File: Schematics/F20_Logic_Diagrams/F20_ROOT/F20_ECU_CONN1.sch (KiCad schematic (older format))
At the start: 1 part

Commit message: 02/18/20 update
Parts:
- gave numbers to parts that had none: 1
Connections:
- no-connect marks 0 -> 10
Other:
- moved on the sheet: U2
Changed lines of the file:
@@
 $Descr A 11000 8500
 encoding utf-8
-Sheet 3 11
+Sheet 3 13
 Title "ECU Connector 1"
 Date ""
@@
 $EndDescr
 $Comp
-L FSAE_Library:ECU_Conn1 U?
+L FSAE_Library:ECU_Conn1 U2
 U 1 1 5E3C649A
-P 4000 1000
-F 0 "U?" H 4750 1173 50  0000 C CNN
-F 1 "ECU_Conn1" H 4750 1150 50  0001 C CNN
-F 2 "" H 4500 2000 50  0001 C CNN
-F 3 "" H 4500 2000 50  0001 C CNN
-F 4 "https://www.molex.com/molex/products/part-detail/pcb_headers/0313872034" H 3950 1400 50  0001 C CNN "Header Datasheet"
-F 5 "https://www.molex.com/molex/products/part-detail/crimp_housings/0345660203" H 4000 1500 50  0001 C CNN "Plug Datasheet"
-	1    4000 1000
+P 4500 1000
+F 0 "U2" H 5250 1173 50  0000 C CNN
+F 1 "ECU_Conn1" H 5250 1150 50  0001 C CNN
+F 2 "" H 5000 2000 50  0001 C CNN
+F 3 "" H 5000 2000 50  0001 C CNN
+F 4 "https://www.molex.com/molex/products/part-detail/pcb_headers/0313872034" H 4450 1400 50  0001 C CNN "Header Datasheet"
+F 5 "https://www.molex.com/molex/products/part-detail/crimp_housings/0345660203" H 4500 1500 50  0001 C CNN "Plug Datasheet"
+	1    4500 1000
 	1    0    0    -1
 $EndComp
-Text GLabel 7500 1450 2    50   Output ~ 0
+Text GLabel 8000 1450 2    50   Output ~ 0
 ECU_+5V_Aux_Out1
-Text GLabel 2000 1450 0    50   Output ~ 0
+Text GLabel 2500 1450 0    50   Output ~ 0
 O2_SNSR_HEAT
-Text GLabel 2000 1900 0    50   Output ~ 0
+Text GLabel 2500 1900 0    50   Output ~ 0
 OS_SNSR_NVOLT
-Text GLabel 2000 1750 0    50   Output ~ 0
+Text GLabel 2500 1750 0    50   Output ~ 0
 O2_SNSR_IPUMP
-Text GLabel 2000 2050 0    50   Output ~ 0
+Text GLabel 2500 2050 0    50   Output ~ 0
 O2_SNSR_VGND
-Text GLabel 2000 1600 0    50   Output ~ 0
+Text GLabel 2500 1600 0    50   Output ~ 0
 O2_SNSR_ITRIM
 Wire Wire Line
-	2000 1450 4000 1450
+	2500 1450 4500 1450
 Wire Wire Line
-	4000 1600 2000 1600
+	4500 1600 2500 1600
 Wire Wire Line
-	2000 1750 4000 1750
+	2500 1750 4500 1750
 Wire Wire Line
-	4000 1900 2000 1900
+	4500 1900 2500 1900
 Wire Wire Line
-	2000 2050 4000 2050
+	2500 2050 4500 2050
 Wire Wire Line
-	7500 1450 5500 1450
+	8000 1450 6000 1450
 Wire Wire Line
-	5500 4450 7000 4450
+	6000 4450 7500 4450
 Wire Wire Line
-	5500 4900 7000 4900
+	6000 4900 7500 4900
 Wire Wire Line
-	7000 4900 7000 4450
-Connection ~ 7000 4450
+	7500 4900 7500 4450
+Connection ~ 7500 4450
 Wire Wire Line
-	7000 4450 7500 4450
-Text GLabel 7500 4450 2    50   Input ~ 0
+	7500 4450 8000 4450
+Text GLabel 8000 4450 2    50   Input ~ 0
 ECU_+12V_RLY
-Text GLabel 2000 5200 0    50   Input ~ 0
+Text GLabel 2500 5200 0    50   Input ~ 0
 ECU_RLY_CTRL_OUT
 Wire Wire Line
-	2000 5200 4000 5200
+	2500 5200 4500 5200
 $Comp
-L FSAE_Library:GND_BAT #PWR?
+L FSAE_Library:GND_BAT #PWR02
 U 1 1 5E44A710
-P 7500 6500
-F 0 "#PWR?" H 7500 6250 50  0001 C CNN
-F 1 "GND_BAT" H 7505 6327 50  0000 C CNN
-F 2 "" H 7500 6500 50  0001 C CNN
-F 3 "" H 7500 6500 50  0001 C CNN
-	1    7500 6500
+P 6500 6450
+F 0 "#PWR02" H 6500 6200 50  0001 C CNN
+F 1 "GND_BAT" H 6505 6277 50  0000 C CNN
+F 2 "" H 6500 6450 50  0001 C CNN
+F 3 "" H 6500 6450 50  0001 C CNN
+	1    6500 6450
 	1    0    0    -1
 $EndComp
 Wire Wire Line
-	7500 6500 7500 6250
+	6500 6450 6500 6250
 Wire Wire Line
-	7500 6250 6000 6250
+	6000 3550 6500 3550
 Wire Wire Line
-	5500 3550 6000 3550
+	6500 3550 6500 4300
+Connection ~ 6500 6250
 Wire Wire Line
-	6000 3550 6000 4300
-Connection ~ 6000 6250
+	6500 6250 6000 6250
 Wire Wire Line
-	6000 6250 5500 6250
+	6000 4300 6500 4300
+Connection ~ 6500 4300
 Wire Wire Line
-	5500 4300 6000 4300
-Connection ~ 6000 4300
+	4500 5350 4000 5350
 Wire Wire Line
-	6000 4300 6000 6250
-Wire Wire Line
-	4000 5350 3500 5350
-Wire Wire Line
-	3500 5350 3500 6500
+	4000 5350 4000 6500
 $Comp
-L FSAE_Library:GND_BAT #PWR?
+L FSAE_Library:GND_BAT #PWR03
 U 1 1 5E4538FC
-P 3500 6500
-F 0 "#PWR?" H 3500 6250 50  0001 C CNN
-F 1 "GND_BAT" H 3505 6327 50  0000 C CNN
-F 2 "" H 3500 6500 50  0001 C CNN
-F 3 "" H 3500 6500 50  0001 C CNN
-	1    3500 6500
+P 4000 6500
+F 0 "#PWR03" H 4000 6250 50  0001 C CNN
+F 1 "GND_BAT" H 4005 6327 50  0000 C CNN
+F 2 "" H 4000 6500 50  0001 C CNN
+F 3 "" H 4000 6500 50  0001 C CNN
+	1    4000 6500
 	1    0    0    -1
 $EndComp
-Text GLabel 2000 2350 0    50   Input ~ 0
+Text GLabel 2500 2350 0    50   Input ~ 0
 ECU_+12V_BAT
 Wire Wire Line
-	2000 2350 4000 2350
+	2500 2350 4500 2350
 Wire Wire Line
-	5500 5050 7500 5050
-Text Notes 8150 5200 0    50   ~ 0
+	6000 5050 8000 5050
+Text Notes 8650 5200 0    50   ~ 0
 SEEMS LIKE ITS JUST CONNECTED\nSTRAIGHT TO BATTERY...\nONE PART IN ECU DOC SAYS PUT 3A FUSE\nBUT IN OTHER THERE IS NO FUSE ...
-Text GLabel 7500 5050 2    50   Input ~ 0
+Text GLabel 8000 5050 2    50   Input ~ 0
 ECU_+12V_IGN
+NoConn ~ 6000 6100
+Wire Wire Line
+	6500 4300 6500 6250
+NoConn ~ 6000 5950
+NoConn ~ 6000 5800
+NoConn ~ 6000 5650
+NoConn ~ 6000 3700
+NoConn ~ 6000 3850
+NoConn ~ 6000 3400
+NoConn ~ 6000 3250
+NoConn ~ 4500 3100
+NoConn ~ 4500 3250
 $EndSCHEMATC

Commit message: 02/19/20 update
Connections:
- net COIL4_CTRL: now reaches U2.11 (Coil3_Out)
- net COIL3_CTRL: now reaches U2.12 (Coil2_Out)
- net COIL2_CTRL: now reaches U2.13 (Coil1_Out)
- net COIL1_CTRL: now reaches U2.14 (Coil0_Out)
- net ECU_+5V_Aux_Out1: no longer names the net of U2.41 (+5V_Aux_Out)
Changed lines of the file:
@@
 	1    0    0    -1
 $EndComp
-Text GLabel 8000 1450 2    50   Output ~ 0
-ECU_+5V_Aux_Out1
 Text GLabel 2500 1450 0    50   Output ~ 0
 O2_SNSR_HEAT
@@
 Wire Wire Line
 	2500 2050 4500 2050
-Wire Wire Line
-	8000 1450 6000 1450
 Wire Wire Line
 	6000 4450 7500 4450
@@
 NoConn ~ 4500 3100
 NoConn ~ 4500 3250
+Text GLabel 2500 2950 0    50   Output ~ 0
+COIL1_CTRL
+Text GLabel 2500 2800 0    50   Output ~ 0
+COIL2_CTRL
+Text GLabel 2500 2650 0    50   Output ~ 0
+COIL3_CTRL
+Text GLabel 2500 2500 0    50   Output ~ 0
+COIL4_CTRL
+Wire Wire Line
+	2500 2500 4500 2500
+Wire Wire Line
+	4500 2650 2500 2650
+Wire Wire Line
+	2500 2800 4500 2800
+Wire Wire Line
+	4500 2950 2500 2950
 $EndSCHEMATC

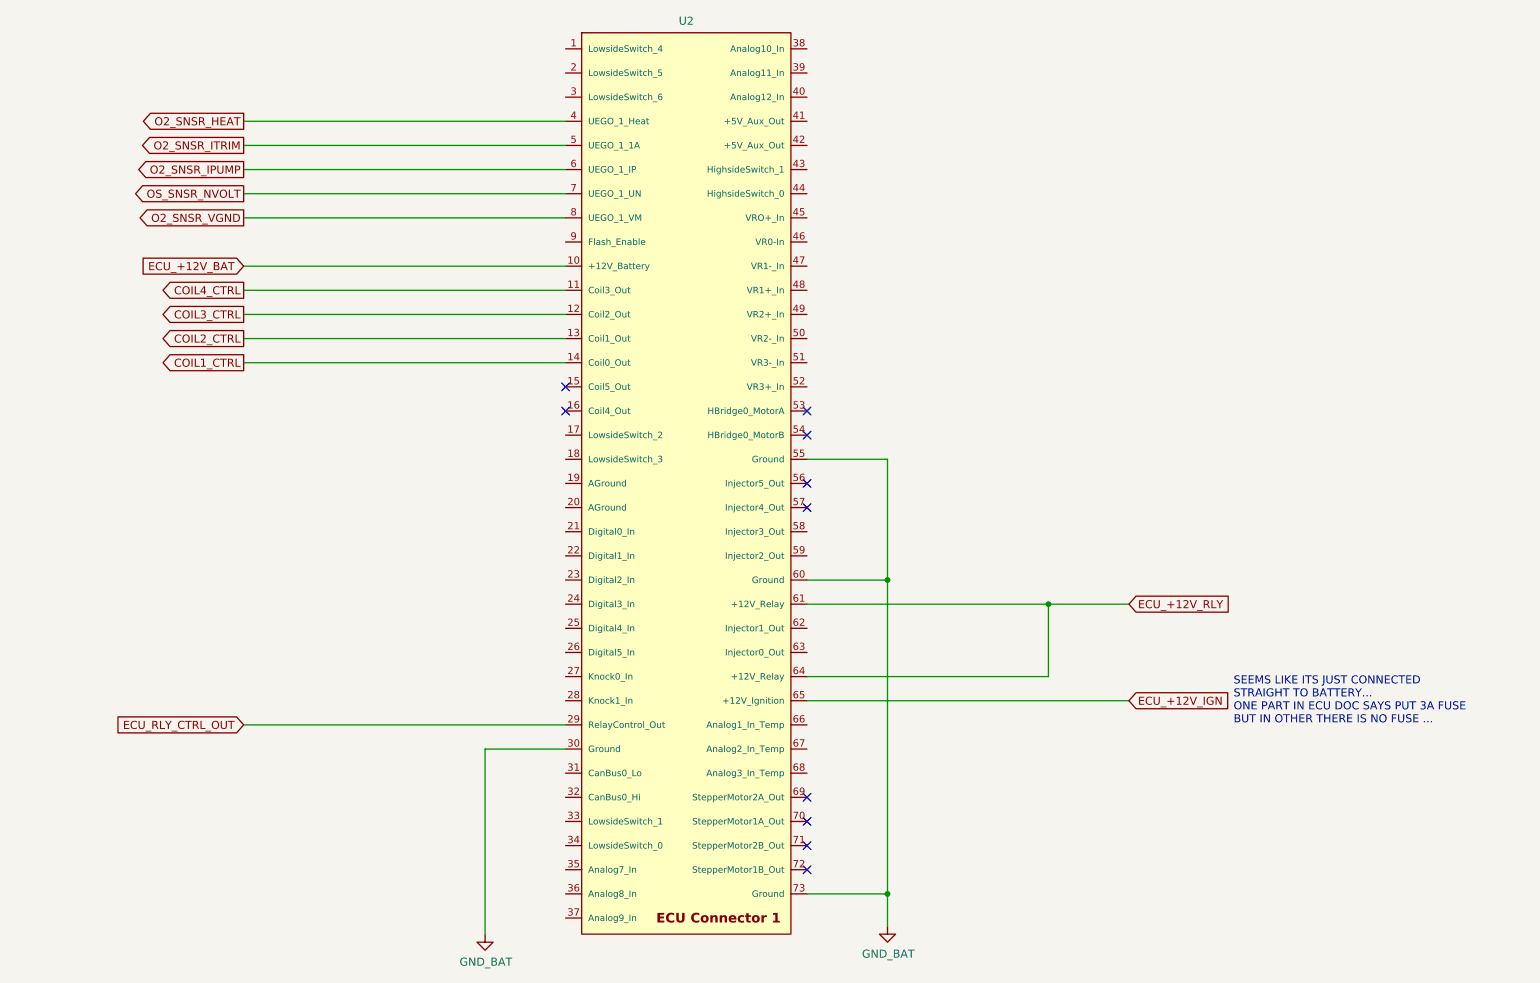
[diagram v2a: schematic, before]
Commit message: Added injectors drawing
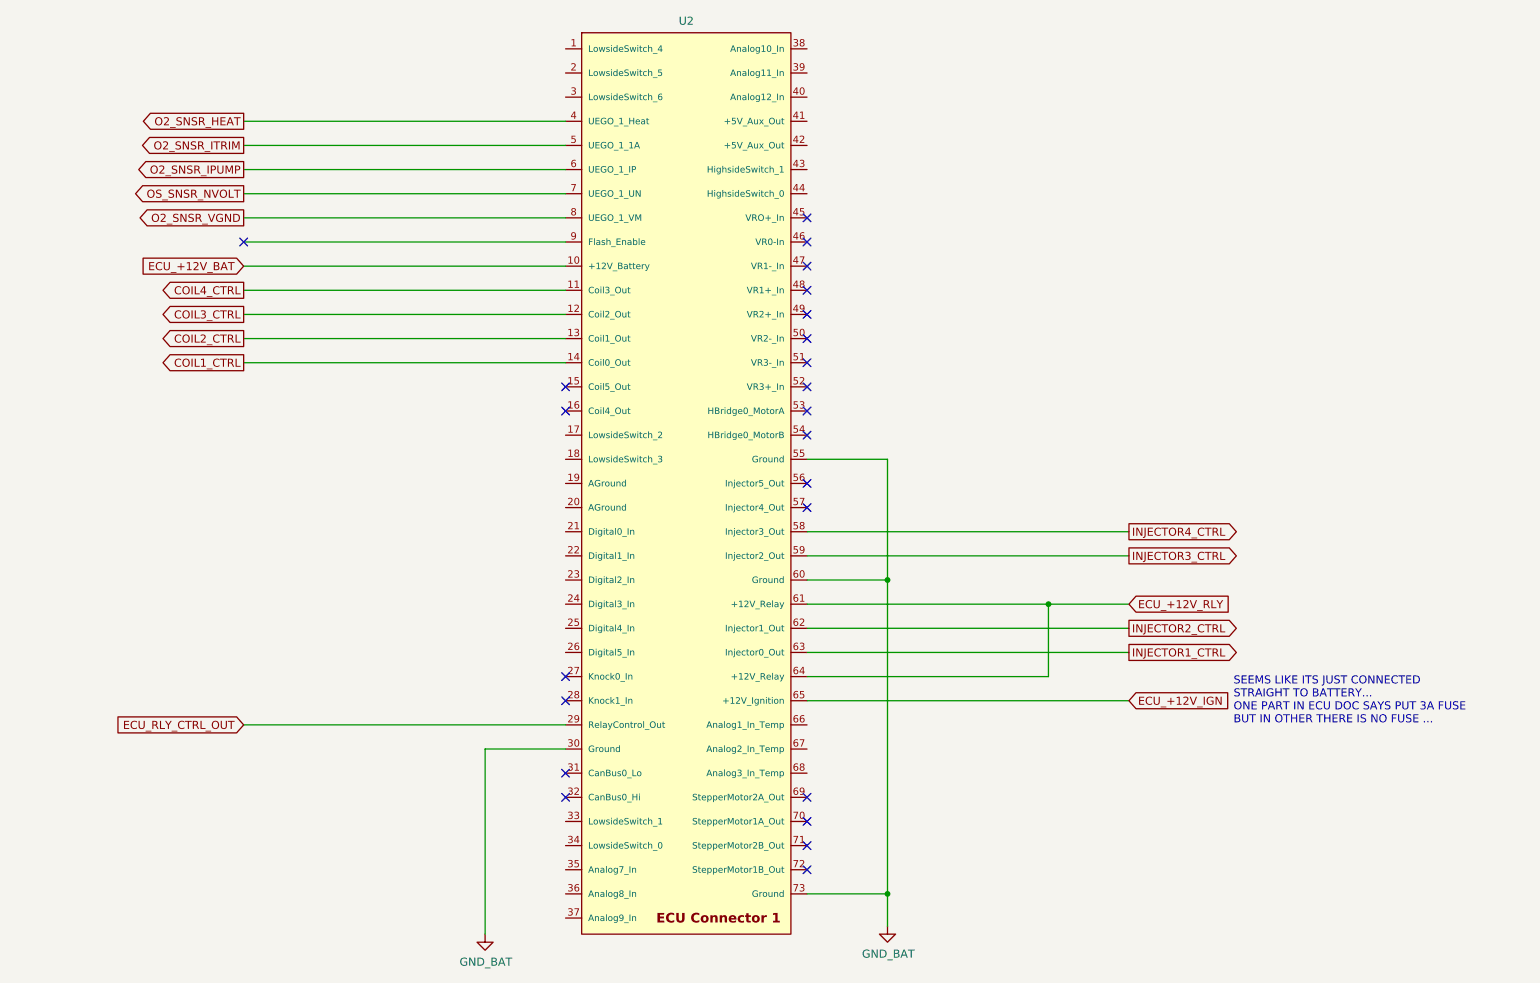
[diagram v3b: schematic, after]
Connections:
- net INJECTOR4_CTRL: now reaches U2.58 (Injector3_Out)
- net INJECTOR3_CTRL: now reaches U2.59 (Injector2_Out)
- net INJECTOR2_CTRL: now reaches U2.62 (Injector1_Out)
- net INJECTOR1_CTRL: now reaches U2.63 (Injector0_Out)
- no-connect marks 10 -> 23
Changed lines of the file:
@@
 $Descr A 11000 8500
 encoding utf-8
-Sheet 3 13
+Sheet 3 14
 Title "ECU Connector 1"
 Date ""
@@
 Wire Wire Line
 	4500 2950 2500 2950
+Wire Wire Line
+	4500 2200 2500 2200
+NoConn ~ 2500 2200
+NoConn ~ 4500 5050
+NoConn ~ 4500 4900
+NoConn ~ 4500 5500
+NoConn ~ 4500 5650
+NoConn ~ 6000 3100
+NoConn ~ 6000 2950
+NoConn ~ 6000 2800
+NoConn ~ 6000 2650
+NoConn ~ 6000 2050
+NoConn ~ 6000 2200
+NoConn ~ 6000 2350
+NoConn ~ 6000 2500
+Wire Wire Line
+	6000 4750 8000 4750
+Wire Wire Line
+	6000 4600 8000 4600
+Wire Wire Line
+	6000 4150 8000 4150
+Wire Wire Line
+	6000 4000 8000 4000
+Text GLabel 8000 4750 2    50   Output ~ 0
+INJECTOR1_CTRL
+Text GLabel 8000 4150 2    50   Output ~ 0
+INJECTOR3_CTRL
+Text GLabel 8000 4000 2    50   Output ~ 0
+INJECTOR4_CTRL
+Text GLabel 8000 4600 2    50   Output ~ 0
+INJECTOR2_CTRL
 $EndSCHEMATC

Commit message: Added steering wheel drawing, udpated some ECU pinout to match previous tune, added accel/XBEE drawing
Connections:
- net SHIFT_UP_BTN: now reaches U2.21 (Digital0_In)
- net SHIFT_DOWN_BTN: now reaches U2.22 (Digital1_In)
- net CLUTCH_BTN: now reaches U2.23 (Digital2_In)
- net BL_SW: now reaches U2.24 (Digital3_In)
- net BL_SIG: now reaches U2.3 (LowsideSwitch_6)
- net CANL: now reaches U2.31 (CanBus0_Lo)
- net CANH: now reaches U2.32 (CanBus0_Hi)
- net TPS_SIG: now reaches U2.35 (Analog7_In)
- net MAP_SIG: now reaches U2.36 (Analog8_In)
- net ECT_SIG: now reaches U2.66 (Analog1_In_Temp)
- net IAT_SIG: now reaches U2.67 (Analog2_In_Temp)
- net O2_SNSR_HEAT: no longer names the net of U2.4 (UEGO_1_Heat)
- net O2_SNSR_IPUMP: no longer names the net of U2.6 (UEGO_1_IP)
- net O2_SNSR_ITRIM: no longer names the net of U2.5 (UEGO_1_1A)
- net O2_SNSR_VGND: no longer names the net of U2.8 (UEGO_1_VM)
- net OS_SNSR_NVOLT: no longer names the net of U2.7 (UEGO_1_UN)
- no-connect marks 23 -> 21
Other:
- note added: "Channel A"
- note added: "Connect to a harness"
- note added: "Shift up\nShift down\nClutch"
- note removed: "SEEMS LIKE ITS JUST CONNECTED\nSTRAIGHT TO BATTERY...\nONE PART IN ECU DOC SAYS PUT 3A FUSE\nBUT IN OTHER THERE IS NO FUSE ..."
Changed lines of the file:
@@
 EESchema Schematic File Version 4
+LIBS:F20_ROOT-cache
 EELAYER 30 0
 EELAYER END
 $Descr A 11000 8500
 encoding utf-8
-Sheet 3 15
+Sheet 3 18
 Title "ECU Connector 1"
 Date ""
@@
 	1    0    0    -1
 $EndComp
-Text GLabel 2500 1450 0    50   Output ~ 0
-O2_SNSR_HEAT
-Text GLabel 2500 1900 0    50   Output ~ 0
-OS_SNSR_NVOLT
-Text GLabel 2500 1750 0    50   Output ~ 0
-O2_SNSR_IPUMP
-Text GLabel 2500 2050 0    50   Output ~ 0
-O2_SNSR_VGND
-Text GLabel 2500 1600 0    50   Output ~ 0
-O2_SNSR_ITRIM
-Wire Wire Line
-	2500 1450 4500 1450
-Wire Wire Line
-	4500 1600 2500 1600
-Wire Wire Line
-	2500 1750 4500 1750
-Wire Wire Line
-	4500 1900 2500 1900
-Wire Wire Line
-	2500 2050 4500 2050
 Wire Wire Line
 	6000 4450 7500 4450
@@
 Wire Wire Line
 	6000 5050 8000 5050
-Text Notes 8650 5200 0    50   ~ 0
-SEEMS LIKE ITS JUST CONNECTED\nSTRAIGHT TO BATTERY...\nONE PART IN ECU DOC SAYS PUT 3A FUSE\nBUT IN OTHER THERE IS NO FUSE ...
 Text GLabel 8000 5050 2    50   Input ~ 0
 ECU_+12V_IGN
@@
 NoConn ~ 4500 5050
 NoConn ~ 4500 4900
-NoConn ~ 4500 5500
-NoConn ~ 4500 5650
 NoConn ~ 6000 3100
 NoConn ~ 6000 2950
@@
 Text GLabel 8000 4600 2    50   Output ~ 0
 INJECTOR2_CTRL
+Text GLabel 2500 5500 0    50   BiDi ~ 0
+CANL
+Wire Wire Line
+	2500 5500 4500 5500
+Text GLabel 2500 5650 0    50   BiDi ~ 0
+CANH
+Wire Wire Line
+	2500 5650 4500 5650
+Text Notes 8150 2150 0    200  ~ 40
+Shift up\nShift down\nClutch
+Text Notes 1550 2250 0    50   ~ 0
+Connect to a harness
+Text Notes 1850 5600 0    50   ~ 0
+Channel A
+Text GLabel 2500 4000 0    50   Input ~ 0
+SHIFT_UP_BTN
+Wire Wire Line
+	2500 4000 4500 4000
+Wire Wire Line
+	4500 4150 2500 4150
+Text GLabel 2500 4150 0    50   Input ~ 0
+SHIFT_DOWN_BTN
+Text GLabel 2500 4300 0    50   Input ~ 0
+CLUTCH_BTN
+Wire Wire Line
+	2500 4300 4500 4300
+Text GLabel 2500 4450 0    50   Input ~ 0
+BL_SW
+Wire Wire Line
+	2500 4450 4500 4450
+Wire Wire Line
+	6000 5350 8000 5350
+Text GLabel 8000 5350 2    50   Input ~ 0
+IAT_SIG
+Wire Wire Line
+	4500 1300 2500 1300
+Text GLabel 2500 1300 0    50   Input ~ 0
+BL_SIG
+Wire Wire Line
+	4500 6100 2500 6100
+Text GLabel 2500 6100 0    50   Input ~ 0
+TPS_SIG
+Wire Wire Line
+	4500 6250 2500 6250
+Text GLabel 2500 6250 0    50   Input ~ 0
+MAP_SIG
+Wire Wire Line
+	6000 5200 8000 5200
+Text GLabel 8000 5200 2    50   Input ~ 0
+ECT_SIG
 $EndSCHEMATC
